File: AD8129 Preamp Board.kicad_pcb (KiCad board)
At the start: 2 copper layers, 50 x 42 mm, 43 parts, among them J1 ANT, J2 TUNE, J3 TRX, T1 Transformer_1P_1S, U1 AD8129, U2 L78L06_SO8

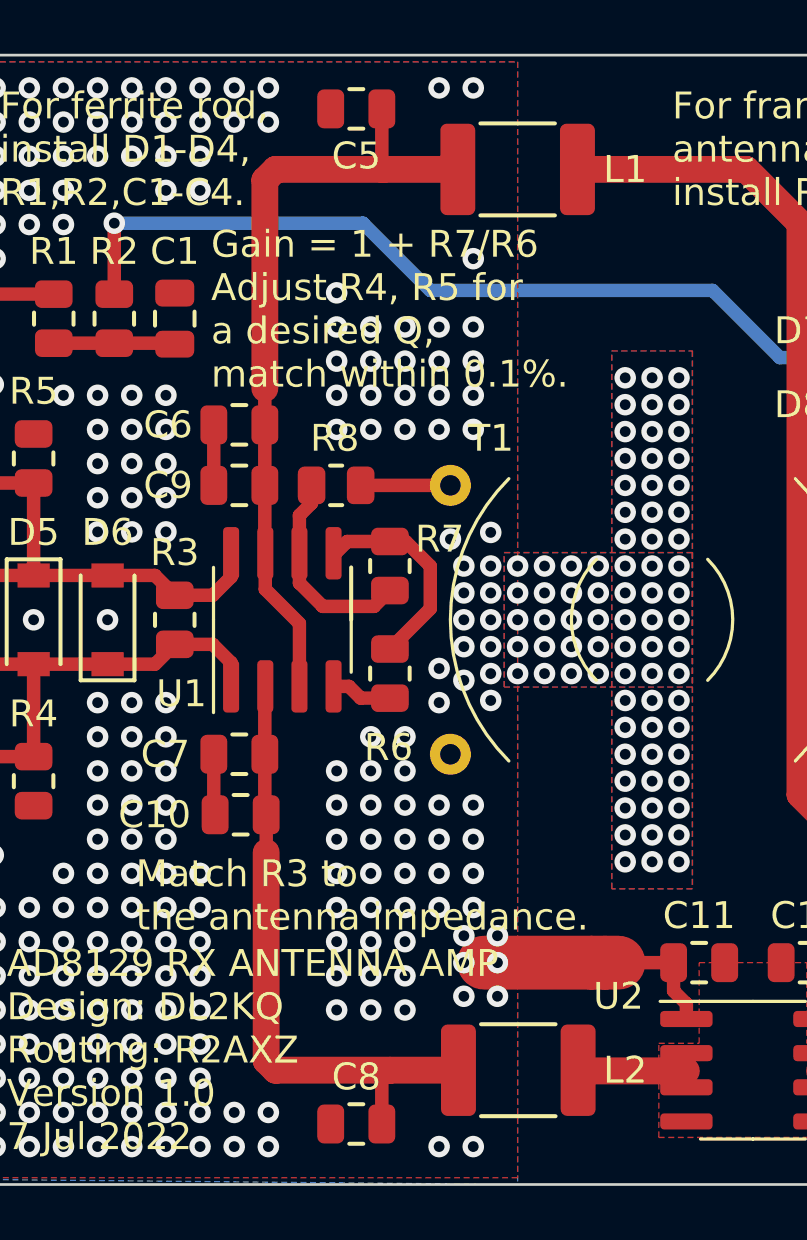
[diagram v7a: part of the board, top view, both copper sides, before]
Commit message: FIX: add vias
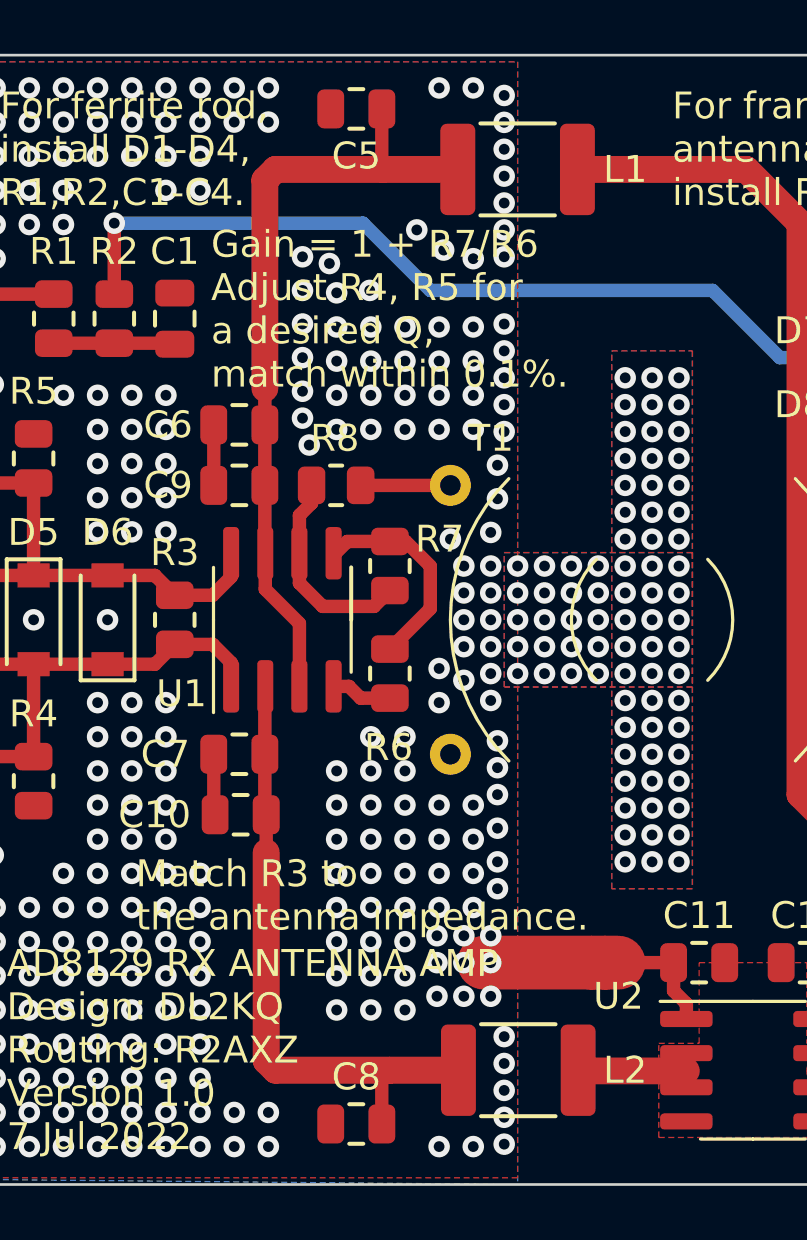
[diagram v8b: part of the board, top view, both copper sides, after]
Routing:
- net GND: vias 347 -> 386
